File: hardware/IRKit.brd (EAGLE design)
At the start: 54 x 56 mm, 71 parts, among them CN1 USB-CONNECTORMICROB, IC1 ATMEGA32U4AU, IC2 TLV70233DBVT, IC3 LM386MM-1, IC4 GS1011MXXS, SW1 EVQPUJ02K, T1 2SD1781K, T2 BSS138

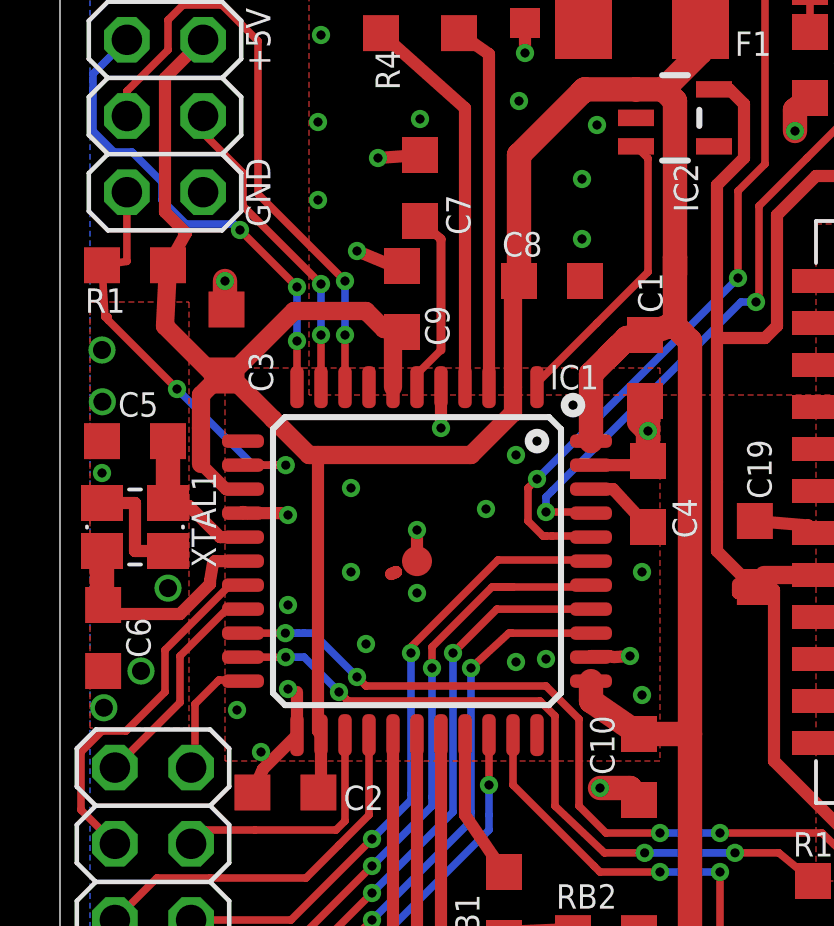
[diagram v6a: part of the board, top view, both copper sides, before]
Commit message: changed C5,C6's value to 12pF
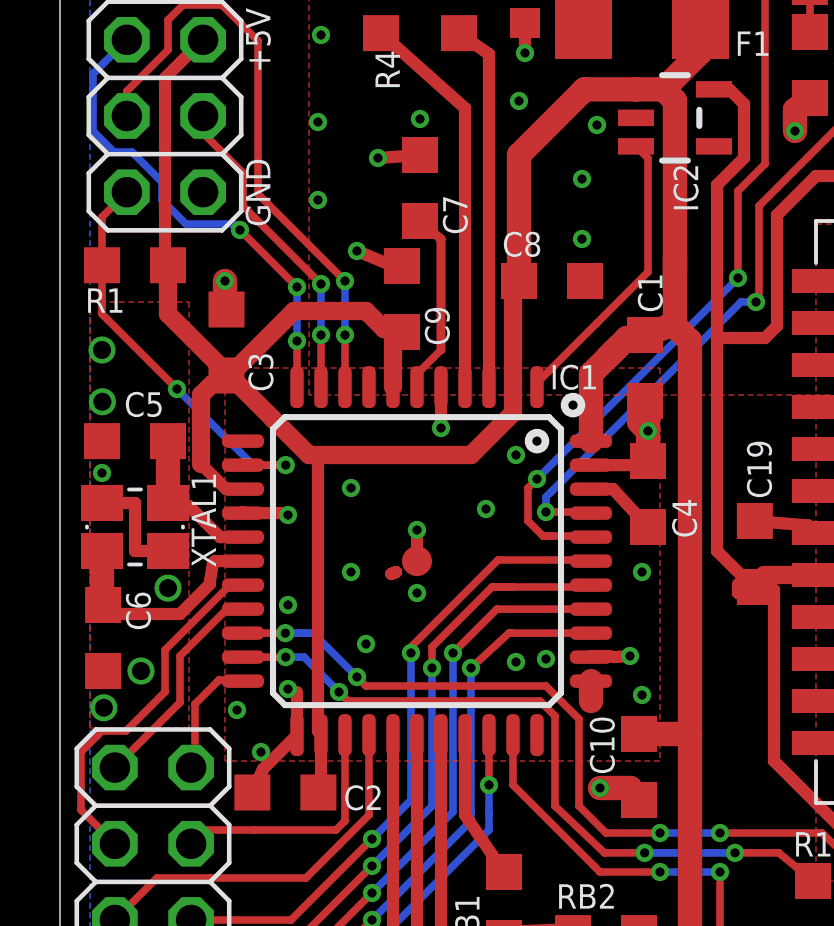
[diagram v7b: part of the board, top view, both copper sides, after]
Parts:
- C5, C6: value 22pF -> 12pF
- XTAL1: value 16MHz -> 16MHz CL:10pF
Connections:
- net XTAL1: now also C6.2, IC1.17, XTAL1.1; no longer C5.2, IC1.16, XTAL1.3
- net XTAL2: now also C5.2, IC1.16, XTAL1.3; no longer C6.2, IC1.17, XTAL1.1
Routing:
- net XTAL2: track 7.91 -> 5.02 mm
- net XTAL1: track 5.02 -> 7.91 mm
- net +5V: track 186.2 -> 183.4 mm
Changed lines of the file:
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@@
 <attribute name="VALUE" x="17.438" y="11.9765" size="0.8128" layer="27"/>
 </element>
-<element name="C5" library="my" package="SMD2012" value="22pF" x="2.5" y="30.6625" smashed="yes">
-<attribute name="NAME" x="1.938" y="31.4785" size="0.8128" layer="25"/>
+<element name="C5" library="my" package="SMD2012" value="12pF" x="2.5" y="30.6625" smashed="yes">
+<attribute name="NAME" x="2.138" y="31.4785" size="0.8128" layer="25"/>
 <attribute name="VALUE" x="1.738" y="28.3765" size="0.8128" layer="27"/>
 </element>
-<element name="C6" library="my" package="SMD2012" value="22pF" x="1.4375" y="24.1" smashed="yes" rot="R90">
-<attribute name="NAME" x="3.0215" y="23.438" size="0.8128" layer="25" rot="R90"/>
+<element name="C6" library="my" package="SMD2012" value="12pF" x="1.4375" y="24.1" smashed="yes" rot="R90">
+<attribute name="NAME" x="3.0215" y="24.338" size="0.8128" layer="25" rot="R90"/>
 <attribute name="VALUE" x="3.7235" y="23.338" size="0.8128" layer="27" rot="R90"/>
 </element>
@@
 </element>
 <element name="C7" library="my" package="SMD2012" value="1uF" x="12" y="39.1" smashed="yes" rot="R270">
-<attribute name="NAME" x="13.684" y="37.538" size="0.8128" layer="25" rot="R90"/>
+<attribute name="NAME" x="13.584" y="37.538" size="0.8128" layer="25" rot="R90"/>
 <attribute name="VALUE" x="9.714" y="39.862" size="0.8128" layer="27" rot="R270"/>
 </element>
@@
 <attribute name="VALUE" x="15.9" y="46.6" size="1.016" layer="27"/>
 </element>
-<element name="XTAL1" library="my" package="CRYSTAL-3.2-2.5" value="16MHz" x="2.5" y="27.8" smashed="yes">
+<element name="XTAL1" library="my" package="CRYSTAL-3.2-2.5" value="16MHz CL:10pF" x="2.5" y="27.8" smashed="yes">
 <attribute name="NAME" x="5.2" y="26.45" size="0.8128" layer="25" rot="R90"/>
 <attribute name="VALUE" x="0.9" y="25.55" size="1.27" layer="27"/>
@@
 <wire x1="6.4375" y1="29.8625" x2="3.9" y2="32.4" width="0.254" layer="16"/>
 <via x="3.9" y="32.4" extent="1-16" drill="0.3048"/>
-<wire x1="1.4" y1="36.525" x2="2.23" y2="36.655" width="0.254" layer="1"/>
-<wire x1="2.23" y1="36.655" x2="2.23" y2="38.96" width="0.254" layer="1"/>
-<wire x1="1.5" y1="34.8" x2="1.4" y2="36.525" width="0.254" layer="1"/>
 <wire x1="1.6" y1="34.7" x2="3.9" y2="32.4" width="0.254" layer="1"/>
-<wire x1="1.6" y1="34.8" x2="1.6" y2="34.7" width="0.254" layer="1"/>
-<wire x1="1.6" y1="34.8" x2="1.5" y2="34.8" width="0.254" layer="1"/>
+<wire x1="1.6" y1="34.7" x2="1.4" y2="34.9" width="0.254" layer="1"/>
+<wire x1="1.4" y1="34.9" x2="1.4" y2="36.525" width="0.254" layer="1"/>
+<wire x1="1.4" y1="36.525" x2="1.4" y2="38.13" width="0.254" layer="1"/>
+<wire x1="1.4" y1="38.13" x2="2.23" y2="38.96" width="0.254" layer="1"/>
 </signal>
 <signal name="+5V" class="1">
@@
 <contactref element="R9" pad="2"/>
 <contactref element="R1" pad="2"/>
-<contactref element="IC1" pad="34"/>
 <contactref element="IC1" pad="44"/>
 <contactref element="C1" pad="2"/>
@@
 <contactref element="C11" pad="1"/>
 <contactref element="C12" pad="+"/>
-<contactref element="C10" pad="2"/>
 <wire x1="8.7" y1="20.8625" x2="8.7" y2="19.4125" width="0.4064" layer="1"/>
 <wire x1="8.7" y1="19.4125" x2="8.6125" y2="18.95" width="0.4064" layer="1"/>
@@
 <wire x1="11.1" y1="32.4625" x2="11.1" y2="34.1" width="0.6096" layer="1"/>
 <wire x1="11.1" y1="34.1" x2="11.4" y2="34.3" width="0.6096" layer="1"/>
-<wire x1="3.6" y1="36.525" x2="4.2" y2="37.6" width="0.4064" layer="1"/>
-<wire x1="4.2" y1="37.6" x2="3.5" y2="38.3" width="0.4064" layer="1"/>
 <wire x1="3.5" y1="38.3" x2="3.5" y2="42.77" width="0.4064" layer="1"/>
 <wire x1="3.5" y1="42.77" x2="4.77" y2="44.04" width="0.4064" layer="1"/>
@@
 <wire x1="20.5" y1="34.5" x2="21" y2="34" width="0.8128" layer="1"/>
 <wire x1="21" y1="34" x2="21" y2="20.9" width="0.8128" layer="1"/>
-<wire x1="19.3" y1="20.9" x2="17.7" y2="22" width="0.8128" layer="1"/>
-<wire x1="17.7" y1="22" x2="17.7" y2="22.6625" width="0.8128" layer="1"/>
 <wire x1="20.5" y1="34.5" x2="20.3" y2="34.5" width="0.8128" layer="1"/>
 <wire x1="18.6" y1="33.8" x2="18.3" y2="33.5" width="0.8128" layer="1"/>
@@
 <wire x1="5.55" y1="32.95" x2="5.75" y2="32.95" width="0.6096" layer="1"/>
 <wire x1="5.75" y1="32.95" x2="7.8" y2="35" width="0.6096" layer="1"/>
-<wire x1="5.55" y1="32.85" x2="5.05" y2="32.95" width="0.6096" layer="1"/>
-<wire x1="5.05" y1="32.95" x2="3.5" y2="34.5" width="0.6096" layer="1"/>
-<wire x1="3.5" y1="34.5" x2="3.6" y2="36.525" width="0.6096" layer="1"/>
 <wire x1="5.1" y1="32.7" x2="5.1" y2="32.6" width="0.4064" layer="1"/>
 <wire x1="5.1" y1="32.7" x2="5.55" y2="32.85" width="0.4064" layer="1"/>
@@
 <wire x1="29.4" y1="47.9" x2="29.8" y2="48.3" width="0.4064" layer="1"/>
 <wire x1="29.8" y1="48.3" x2="29.8" y2="49.975" width="0.4064" layer="1"/>
-<wire x1="19.3" y1="20.9" x2="19.4" y2="20.9" width="0.8128" layer="1"/>
 <wire x1="19.4" y1="20.9" x2="21" y2="20.9" width="0.8128" layer="1"/>
 <wire x1="21" y1="20.9" x2="21" y2="10.3" width="0.8128" layer="1"/>
@@
 <wire x1="15.3" y1="36" x2="15.3" y2="40.2" width="0.8128" layer="1"/>
 <wire x1="15.3" y1="40.2" x2="17.4" y2="42.3" width="0.8128" layer="1"/>
+<contactref element="IC1" pad="34"/>
+<contactref element="C10" pad="2"/>
+<wire x1="17.7" y1="22" x2="17.7" y2="22.6625" width="0.8128" layer="1"/>
+<wire x1="5.55" y1="32.95" x2="3.6" y2="34.9" width="0.6096" layer="1"/>
+<wire x1="3.6" y1="34.9" x2="3.6" y2="36.525" width="0.6096" layer="1"/>
+<wire x1="3.5" y1="38.3" x2="3.5" y2="36.625" width="0.4064" layer="1"/>
+<wire x1="3.5" y1="36.625" x2="3.6" y2="36.525" width="0.4064" layer="1"/>
+<wire x1="19.4" y1="20.9" x2="19.3" y2="20.9" width="0" layer="19" extent="1-1"/>
+<wire x1="17.7" y1="22" x2="19.3" y2="20.9" width="0" layer="19" extent="1-1"/>
 </signal>
 <signal name="N$3">
@@
 </signal>
 <signal name="XTAL1">
-<contactref element="C5" pad="2"/>
-<contactref element="IC1" pad="16"/>
-<contactref element="XTAL1" pad="3"/>
-<wire x1="3.6" y1="30.6625" x2="3.6" y2="28.7" width="0.8128" layer="1"/>
-<wire x1="3.6" y1="28.7" x2="3.6" y2="28.6" width="0.8128" layer="1"/>
-<wire x1="6.1" y1="27.4625" x2="5.3375" y2="27.4625" width="0.4064" layer="1"/>
-<wire x1="5.3375" y1="27.4625" x2="4.3" y2="28.5" width="0.4064" layer="1"/>
-<wire x1="4.3" y1="28.5" x2="3.8" y2="28.5" width="0.4064" layer="1"/>
-<wire x1="3.8" y1="28.5" x2="3.6" y2="28.6" width="0.4064" layer="1"/>
-</signal>
-<signal name="XTAL2">
 <contactref element="C6" pad="2"/>
 <contactref element="IC1" pad="17"/>
@@
 <signal name="N$15">
 </signal>
+<signal name="XTAL2">
+<contactref element="C5" pad="2"/>
+<contactref element="IC1" pad="16"/>
+<contactref element="XTAL1" pad="3"/>
+<wire x1="3.6" y1="30.6625" x2="3.6" y2="28.7" width="0.8128" layer="1"/>
+<wire x1="3.6" y1="28.7" x2="3.6" y2="28.6" width="0.8128" layer="1"/>
+<wire x1="6.1" y1="27.4625" x2="5.3375" y2="27.4625" width="0.4064" layer="1"/>
+<wire x1="5.3375" y1="27.4625" x2="4.3" y2="28.5" width="0.4064" layer="1"/>
+<wire x1="4.3" y1="28.5" x2="3.8" y2="28.5" width="0.4064" layer="1"/>
+<wire x1="3.8" y1="28.5" x2="3.6" y2="28.6" width="0.4064" layer="1"/>
+</signal>
 </signals>
